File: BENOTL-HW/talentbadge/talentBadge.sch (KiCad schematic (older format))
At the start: 62 parts

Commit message: Rename components
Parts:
- removed C?: 0.1uF, symbol C_Small
- added C2: 0.1uF, symbol C_Small
- P1: renamed from P?; symbol USB_A -> USB_A-RESCUE-talentBadge
- Q1, Q2: renamed from Q?; footprint SOT-23 -> (none)
- gave numbers to parts that had none: 58
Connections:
- net +3V3: now also C2.1
- net GND: now also C2.2
- no-connect marks 4 -> 5

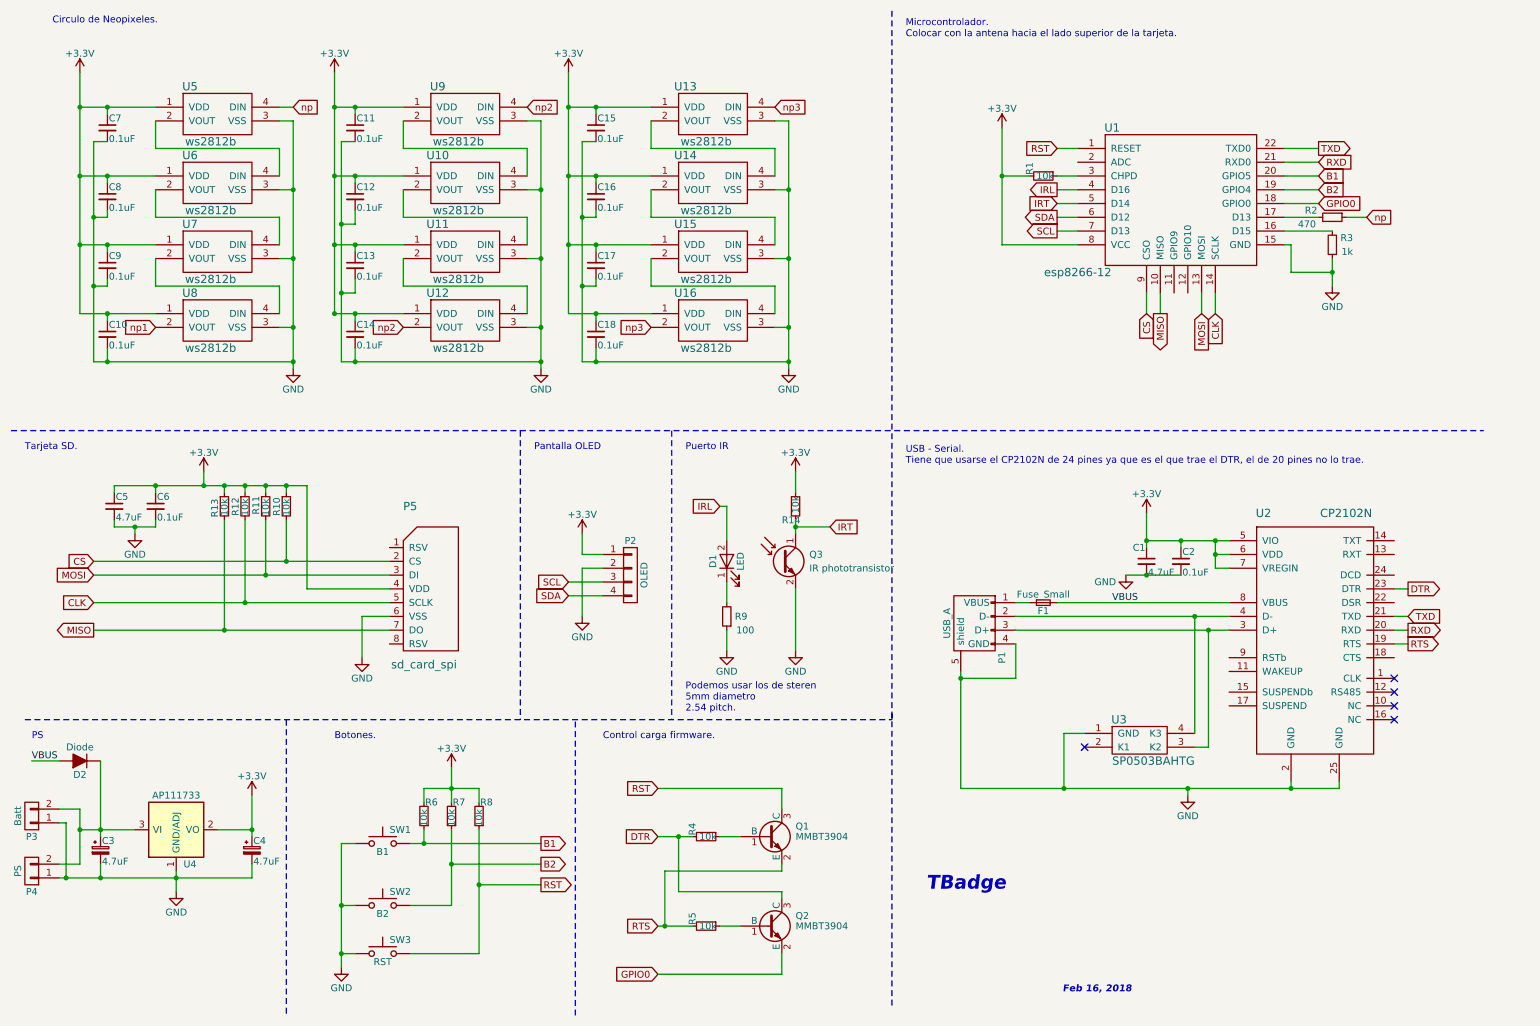
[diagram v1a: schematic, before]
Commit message: Fix neopixel rail and CvPCB
Associated all schematics with its footprints
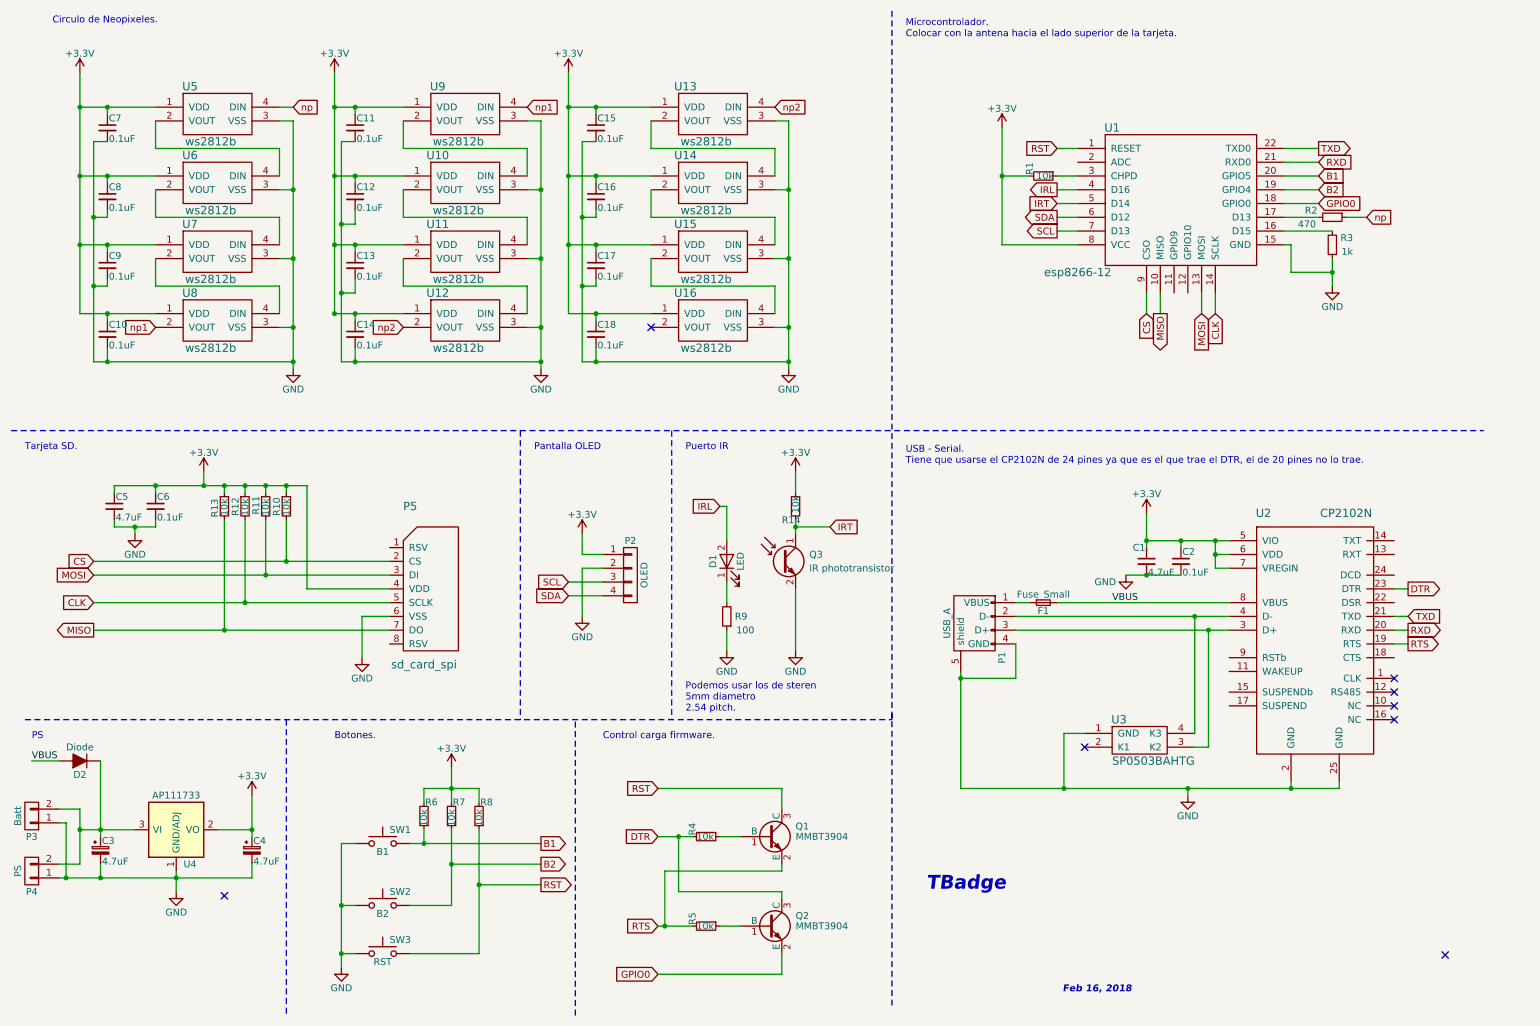
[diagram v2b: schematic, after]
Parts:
- C1, C10, C11, C12, C13, C14, C15, C16, C17, C18, C2, C3, C4, C5, C6, C7, C8, C9: footprint (none) -> Capacitors_SMD:C_0805_HandSoldering
- D1: footprint (none) -> LEDs:LED_D3.0mm
- D2: footprint (none) -> Diodes_SMD:D_SMA
- F1: footprint (none) -> talentBadge:0440.500WRA
- P1: footprint (none) -> talentBadge:629105150921
- P2: footprint (none) -> Pin_Headers:Pin_Header_Straight_1x04_Pitch2.54mm
- P5: footprint (none) -> talentBadge:MOLEX_0475710001
- Q1, Q2, Q3: footprint (none) -> TO_SOT_Packages_SMD:SOT-23
- R1, R10, R11, R12, R13, R14, R2, R3, R4, R5, R6, R7, R8, R9: footprint (none) -> Resistors_SMD:R_0805_HandSoldering
- SW1, SW2, SW3: footprint (none) -> talentBadge:SW_TL3342F160QG
- U1: footprint (none) -> talentBadge:ESP-12E_SMD
- U10, U11, U12, U13, U14, U15, U16, U5, U6, U7, U8, U9: footprint (none) -> LEDs:LED_WS2812B-PLCC4
- U2: footprint (none) -> talentBadge:QFN-24-5x5mm_Pitch0.50mm
- U3: footprint (none) -> talentBadge:SOT143
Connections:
- net np1: now also U9.4 (DIN)
- net np2: now also U13.4 (DIN); no longer U9.4 (DIN)
- net np3: no longer names the net of U16.2 (VOUT)
- net np3: no longer U13.4 (DIN)
- no-connect marks 5 -> 8

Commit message: Add provissional footprints
For IR and BATT and PS
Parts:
- P3, P4: footprint (none) -> Pin_Headers:Pin_Header_Straight_1x02_Pitch2.54mm
- Q3: footprint TO_SOT_Packages_SMD:SOT-23 -> LEDs:LED_D5.0mm
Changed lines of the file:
@@
 F 0 "P3" H 650 6500 50  0000 C CNN
 F 1 "Batt" V 750 6350 50  0000 C CNN
-F 2 "" H 650 6350 50  0001 C CNN
+F 2 "Pin_Headers:Pin_Header_Straight_1x02_Pitch2.54mm" H 650 6350 50  0001 C CNN
 F 3 "" H 650 6350 50  0000 C CNN
 	1    650  6350
@@
 F 0 "P4" H 650 6900 50  0000 C CNN
 F 1 "PS" V 750 6750 50  0000 C CNN
-F 2 "" H 650 6750 50  0001 C CNN
+F 2 "Pin_Headers:Pin_Header_Straight_1x02_Pitch2.54mm" H 650 6750 50  0001 C CNN
 F 3 "" H 650 6750 50  0000 C CNN
 	1    650  6750
@@
 F 0 "Q3" H 6300 4550 50  0000 L CNN
 F 1 "IR phototransistor" H 6300 4450 50  0000 L CNN
-F 2 "TO_SOT_Packages_SMD:SOT-23" H 6300 4600 50  0001 C CNN
+F 2 "LEDs:LED_D5.0mm" H 6300 4600 50  0001 C CNN
 F 3 "" H 6100 4500 50  0000 C CNN
 F 4 "PT1302B/C2" H 6100 4500 60  0001 C CNN "PartNo"
